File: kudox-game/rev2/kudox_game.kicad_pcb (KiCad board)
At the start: 2 copper layers, 145.7 x 130.4 mm, 65 parts, among them K0 KEYSW, K1 KEYSW, K11 KEYSW, K12 KEYSW, K13 KEYSW, K14 KEYSW, K15 KEYSW, K2 KEYSW, K20 KEYSW, K21 KEYSW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

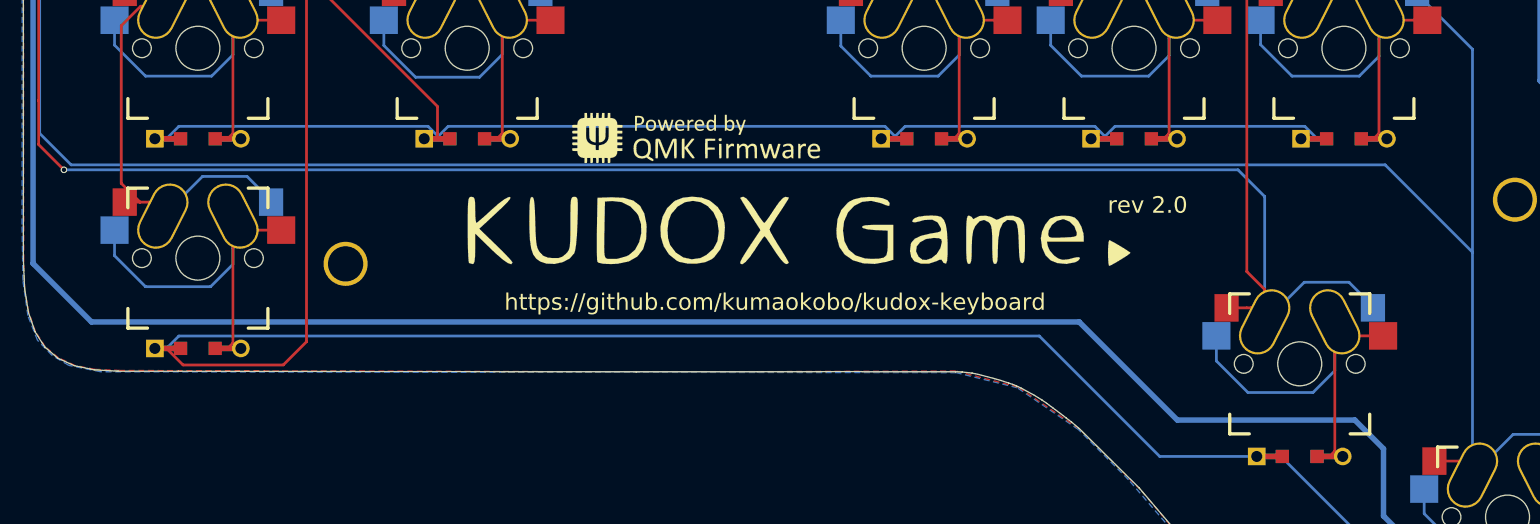
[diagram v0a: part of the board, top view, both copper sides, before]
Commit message: Modified LOGO from silk to metal paste.
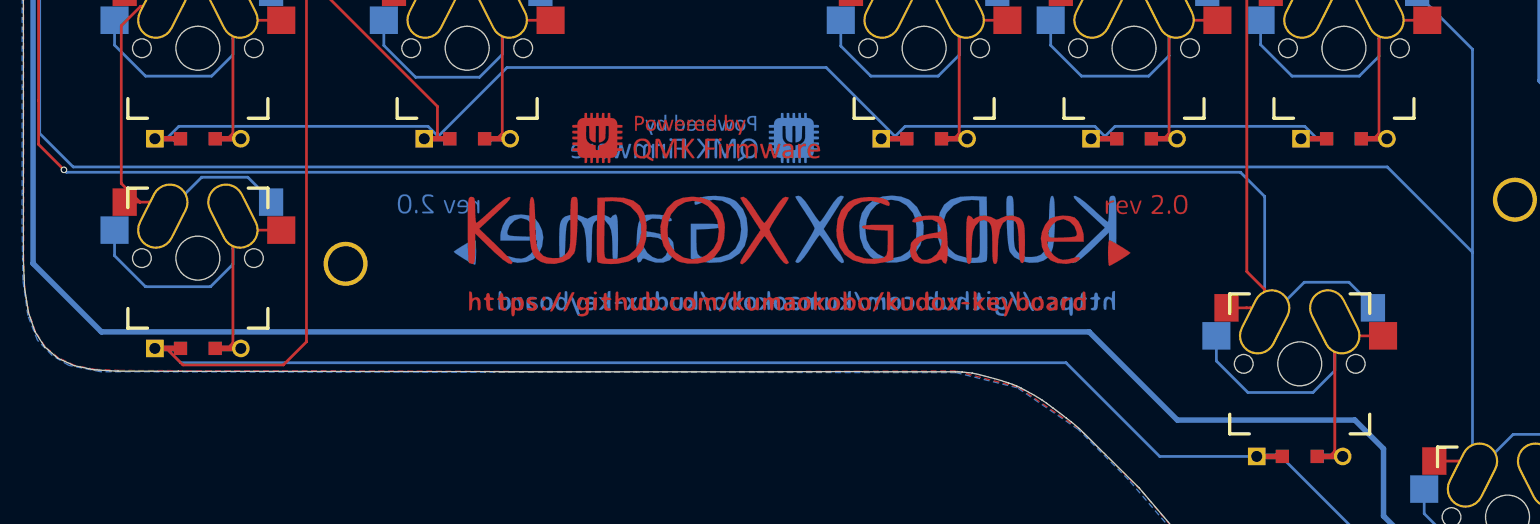
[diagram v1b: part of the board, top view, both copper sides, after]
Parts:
- added G***: kudox_github, kudox_game_footprints:kudox_github, F.Cu at (110.7, 121.1)
- added G***: kudox_github, kudox_game_footprints:kudox_github, B.Cu at (113.4, 121.1)
- added G***: LOGO, kudox_game_footprints:version, F.Cu at (144.2, 112.1)
- added G***: LOGO, kudox_game_footprints:version, B.Cu at (80.0, 112.0)
- G*** (x2): footprint kudox_game_footprints:kudox_game_logo -> kudox_game_footprints:kudox_game_logo_pad
- G*** (x2): footprint kudox_game_footprints:qmk-badge -> kudox_game_footprints:qmk-badge-pad
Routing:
- net row3: track 170.2 -> 174.7 mm
- net row4: track 214.9 -> 214.0 mm
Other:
- board text removed: "https://github.com/kumaokobo/kudox-keyboard"
- board text removed: "rev 2.0"

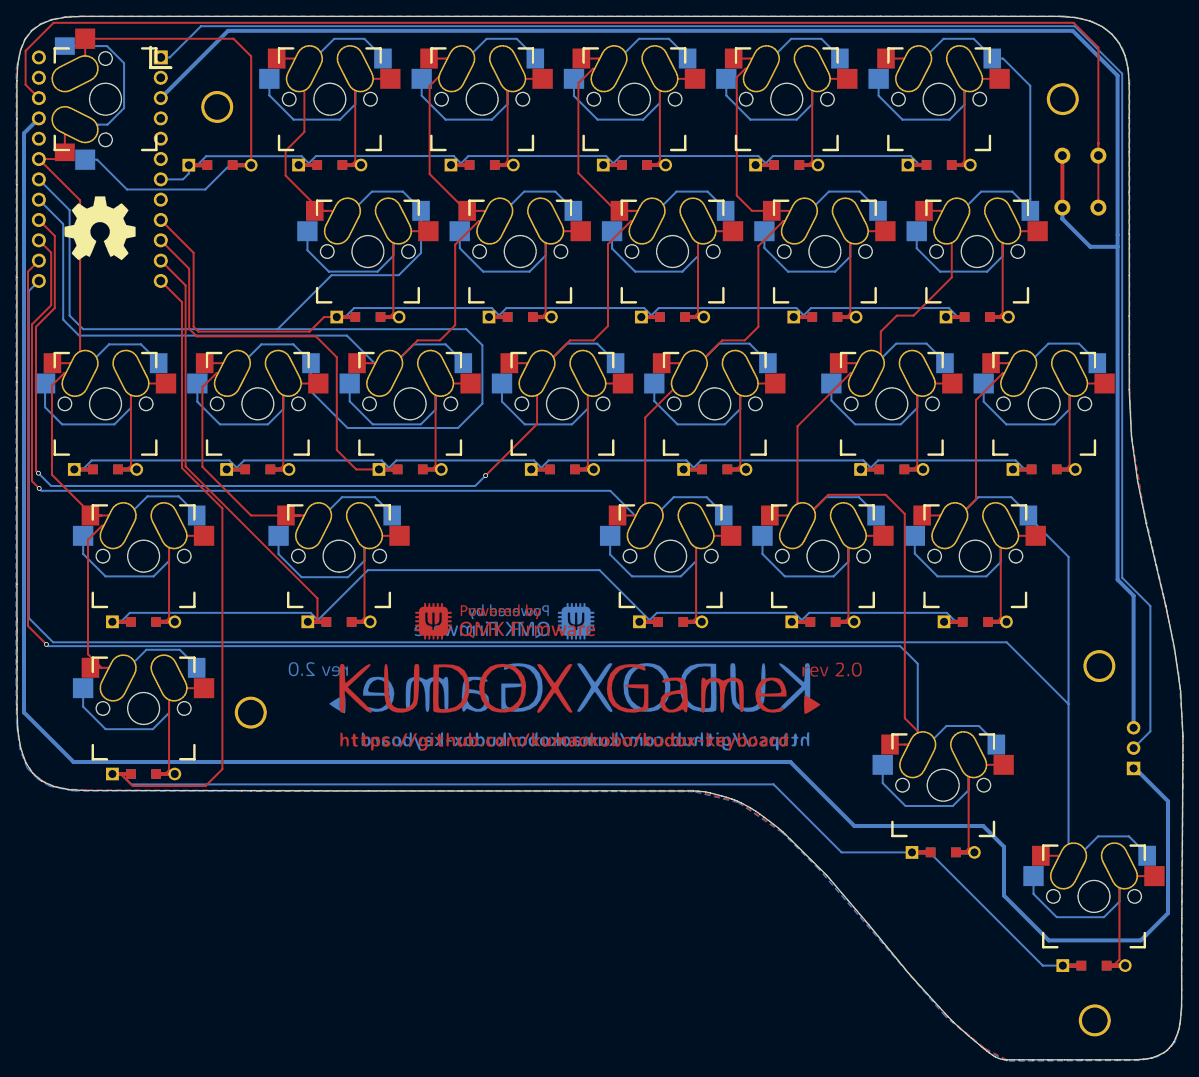
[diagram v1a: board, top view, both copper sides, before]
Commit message: [kudox-game] Modify Kudox Game rev2 using MX socket optional switch foot print. (#45)
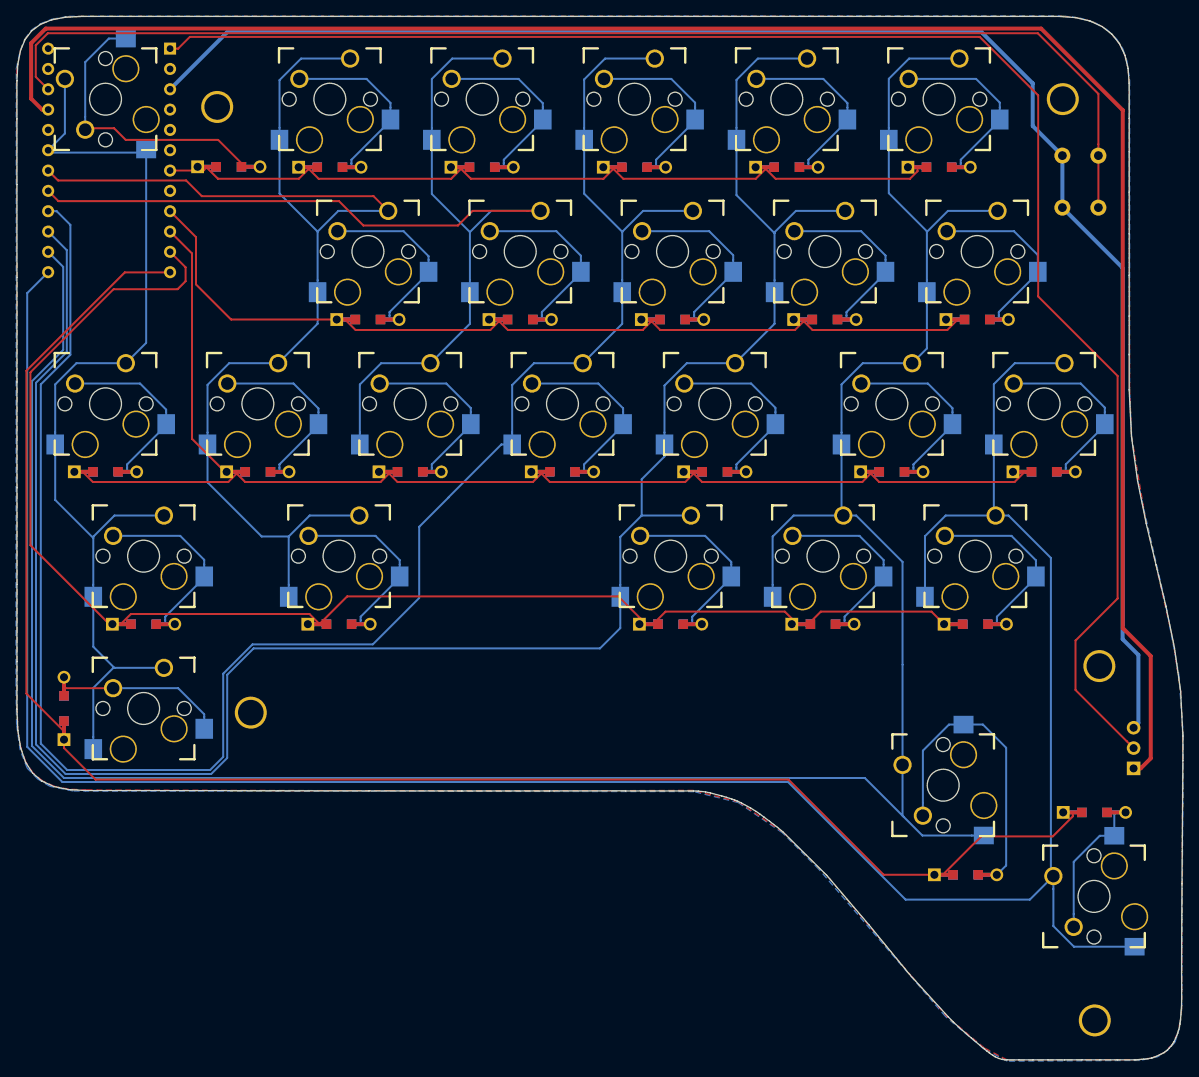
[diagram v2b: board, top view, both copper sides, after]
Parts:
- removed REF***: OSHW-Logo2_14.6x12mm_SilkScreen, Symbols:OSHW-Symbol_8.9x8mm_SilkScreen
- K0, K1, K11, K12, K13, K14, K15, K2, K20, K21, K22, K23, K24, K25, K26, K3, K31, K34, K35, K36, K4, K5: footprint kudox_game_footprints:Mx_hotswappable -> kudox_game_footprints:MX_socket_optional_100
- K30, K40, K45: footprint kudox_game_footprints:Mx_hotswappable -> kudox_game_footprints:MX_socket_optional_150
- K46: footprint kudox_game_footprints:Mx_hotswappable -> kudox_game_footprints:MX_socket_optional_200
- moved D46 19.2 mm to (177.0, 130.0)
- moved D40 12.9 mm to (48.2, 117.0), turned to 270 degrees
- moved D45 3.96 mm to (160.9, 137.8)
- moved U1 1.60 mm to (53.8, 48.5)
- moved D0 1.12 mm to (68.8, 49.3)
- moved D11 0.31 mm to (86.2, 68.4)
- moved D12 0.31 mm to (105.2, 68.4)
- moved D13 0.31 mm to (124.3, 68.4)
- moved D14 0.31 mm to (143.3, 68.4)
- moved D15 0.31 mm to (162.3, 68.4)
- moved D20 0.30 mm to (53.4, 87.4)
- moved D21 0.30 mm to (72.4, 87.4)
- moved D22 0.30 mm to (91.5, 87.4)
- moved D23 0.30 mm to (110.5, 87.4)
- moved D24 0.30 mm to (129.6, 87.4)
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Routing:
- net col1: track 251.9 -> 156.4 mm
- net col5: track 369.8 -> 331.5 mm, vias 1 -> 0
- net col3: track 207.8 -> 235.0 mm, vias 2 -> 0
- net col0: track 151.3 -> 126.1 mm
- net Net-(D0-Pad2): track 62.5 -> 37.5 mm
- net GND: track 224.0 -> 199.7 mm
- net Net-(D46-Pad2): track 38.0 -> 17.6 mm
- net VCC: track 254.8 -> 236.2 mm
- net col2: track 159.3 -> 140.9 mm
- net row2: track 188.4 -> 170.7 mm
- net Net-(D40-Pad2): track 36.5 -> 20.8 mm
- net col4: track 248.7 -> 263.1 mm, vias 1 -> 0
- net Net-(D20-Pad2): track 36.9 -> 22.5 mm
- net Net-(D34-Pad2): track 36.6 -> 22.5 mm
- net Net-(D21-Pad2): track 36.6 -> 22.6 mm
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
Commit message: Modify angle of LED strip hole on kudox-game
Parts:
- moved D46 20.0 mm to (177.0, 150.0)
- moved RGB_STRIP1 6.71 mm to (175.9, 127.5), turned to 310 degrees
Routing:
- net VCC: track 236.2 -> 245.0 mm
- net GND: track 199.7 -> 205.5 mm
- net Net-(D46-Pad2): track 17.6 -> 23.1 mm
- net row4: track 211.1 -> 213.7 mm
- net rgb_data: track 203.0 -> 205.3 mm
